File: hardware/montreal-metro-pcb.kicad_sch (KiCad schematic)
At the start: 95 parts, among them SW1 TS-1187A-B-A-B, SW2 TS-1187A-B-A-B, SW3 TS-1187A-B-A-B, SW4 TS-1187A-B-A-B, U1 XIAO-RP2040-DIP

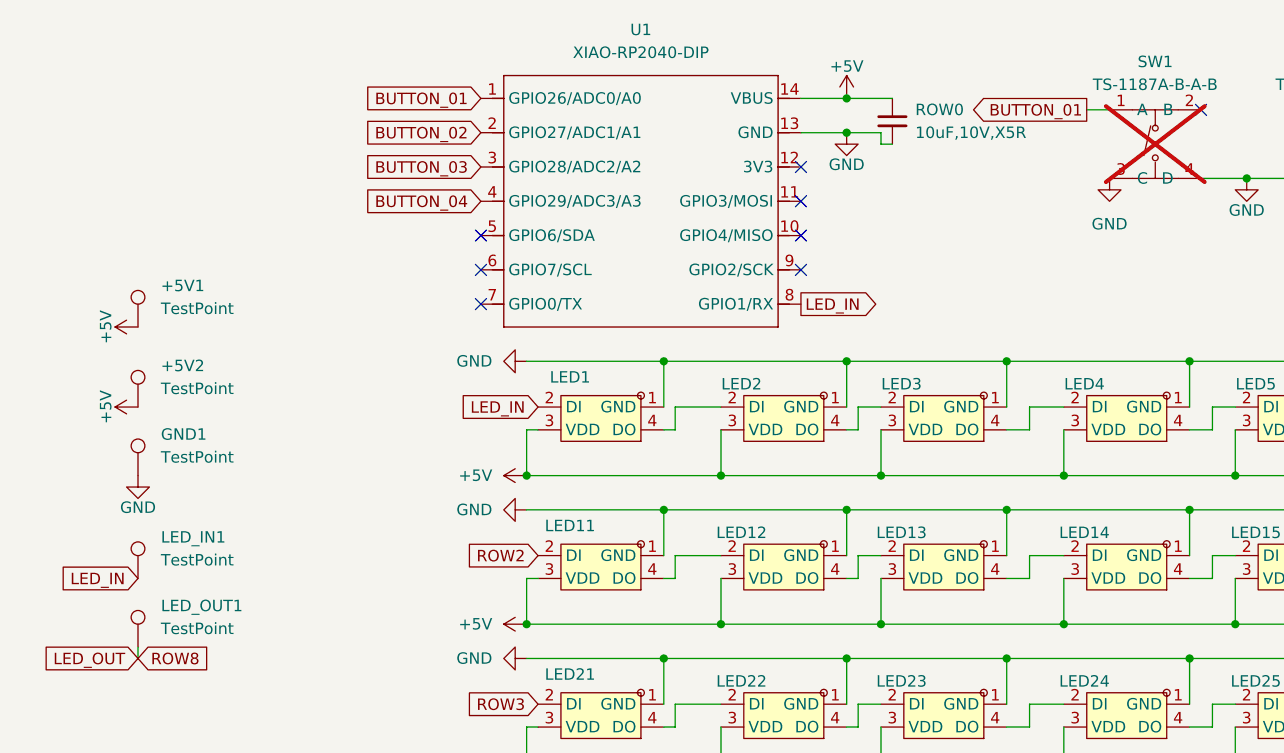
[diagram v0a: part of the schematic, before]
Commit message: Hand-routed board, R1 and C1, owl back art, JLCPCB outputs
The board is now routed by hand with every assembled part on the
top side. Added:

- C1, 100 uF 6.3 V 1206 X5R bulk capacitor (LCSC C15008, basic)
  on the +5V trunk.
- R1, 330 R 0402 (LCSC C25104, basic) in series on the LED data
  line. U1 pin 8 and the LED_IN1 test point are now on LED_DATA;
  LED_IN runs from R1 to LED1 only.
- The snowy-owl artwork on the back silkscreen as the board-only
  footprint LOGO1, generated by the new tools/svg_to_silk.py.
- JLCPCB gerbers, BOM and CPL in hardware/jlcpcb, stamped
  2026-10-18-1117; make_jlcpcb.py takes the stamp as an argument.
- The latest hand label edits, imported and frozen.

DRC: no errors, 0 unconnected, 0 schematic parity issues.

Co-Authored-By: Claude Opus 5.5 <noreply@anthropic.com>
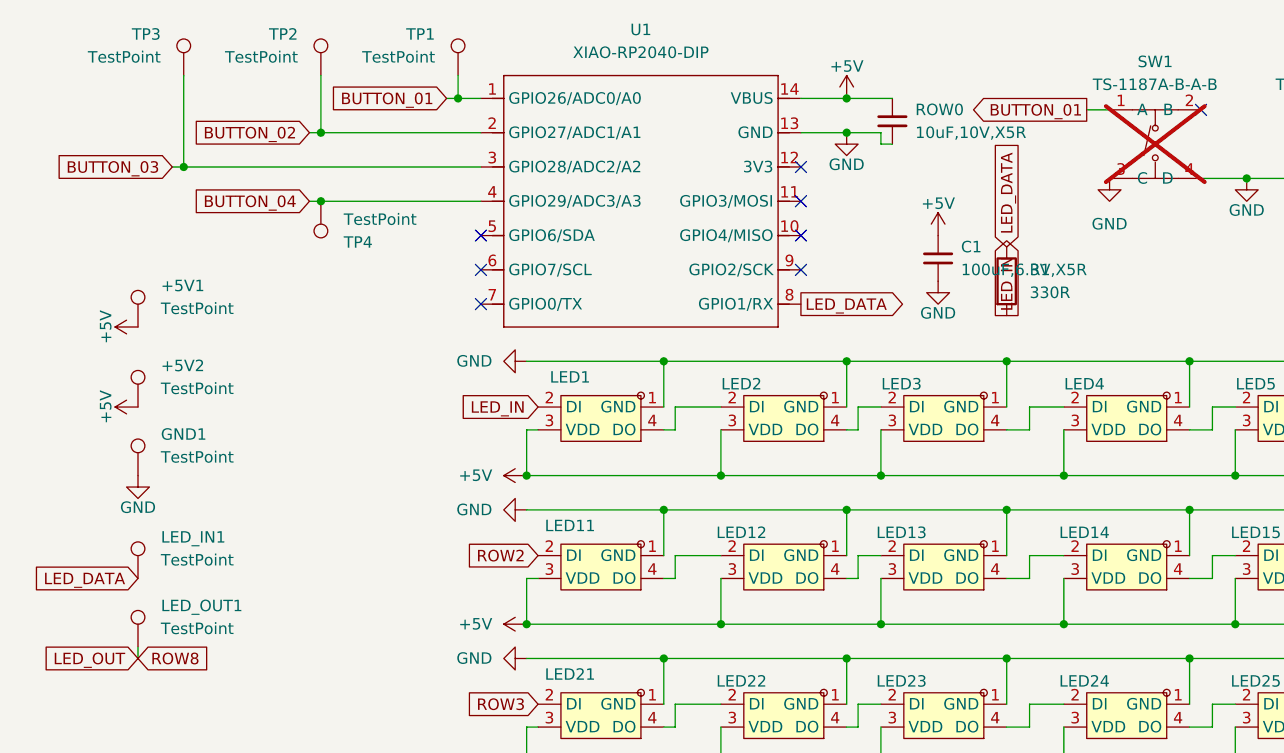
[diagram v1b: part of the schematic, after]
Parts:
- added C1: 100uF,6.3V,X5R, Capacitor_SMD:C_1206_3216Metric, symbol __sws_jlpcb:jlcpcb-1uF,25V,X5R
- added R1: 330R, Resistor_SMD:R_0402_1005Metric, symbol Device:R
- added TP1, TP2, TP3, TP4: TestPoint, TestPoint:TestPoint_Pad_3.0x3.0mm, symbol Connector:TestPoint
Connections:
- net +5V: now also C1.1
- net BUTTON_01: now also TP1.1
- net BUTTON_02: now also TP2.1
- net BUTTON_03: now also TP3.1
- net BUTTON_04: now also TP4.1
- net GND: now also C1.2
- net LED_IN: now also R1.2; no longer LED_IN1.1, U1.8 (GPIO1/RX)
- new net LED_DATA: LED_IN1.1, R1.1, U1.8 (GPIO1/RX)
